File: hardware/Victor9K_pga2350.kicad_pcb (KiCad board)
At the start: 4 copper layers, 232.7 x 126.4 mm, 23 parts, among them IC1 74LVC1G14GW,125, J1 PICO DEBUG, J2 Micro_SD_Card, J4 DX07S016JA1R1500, J5 UART, SW1 BOOTSEL, U1 ESP32-S3-DevKitC

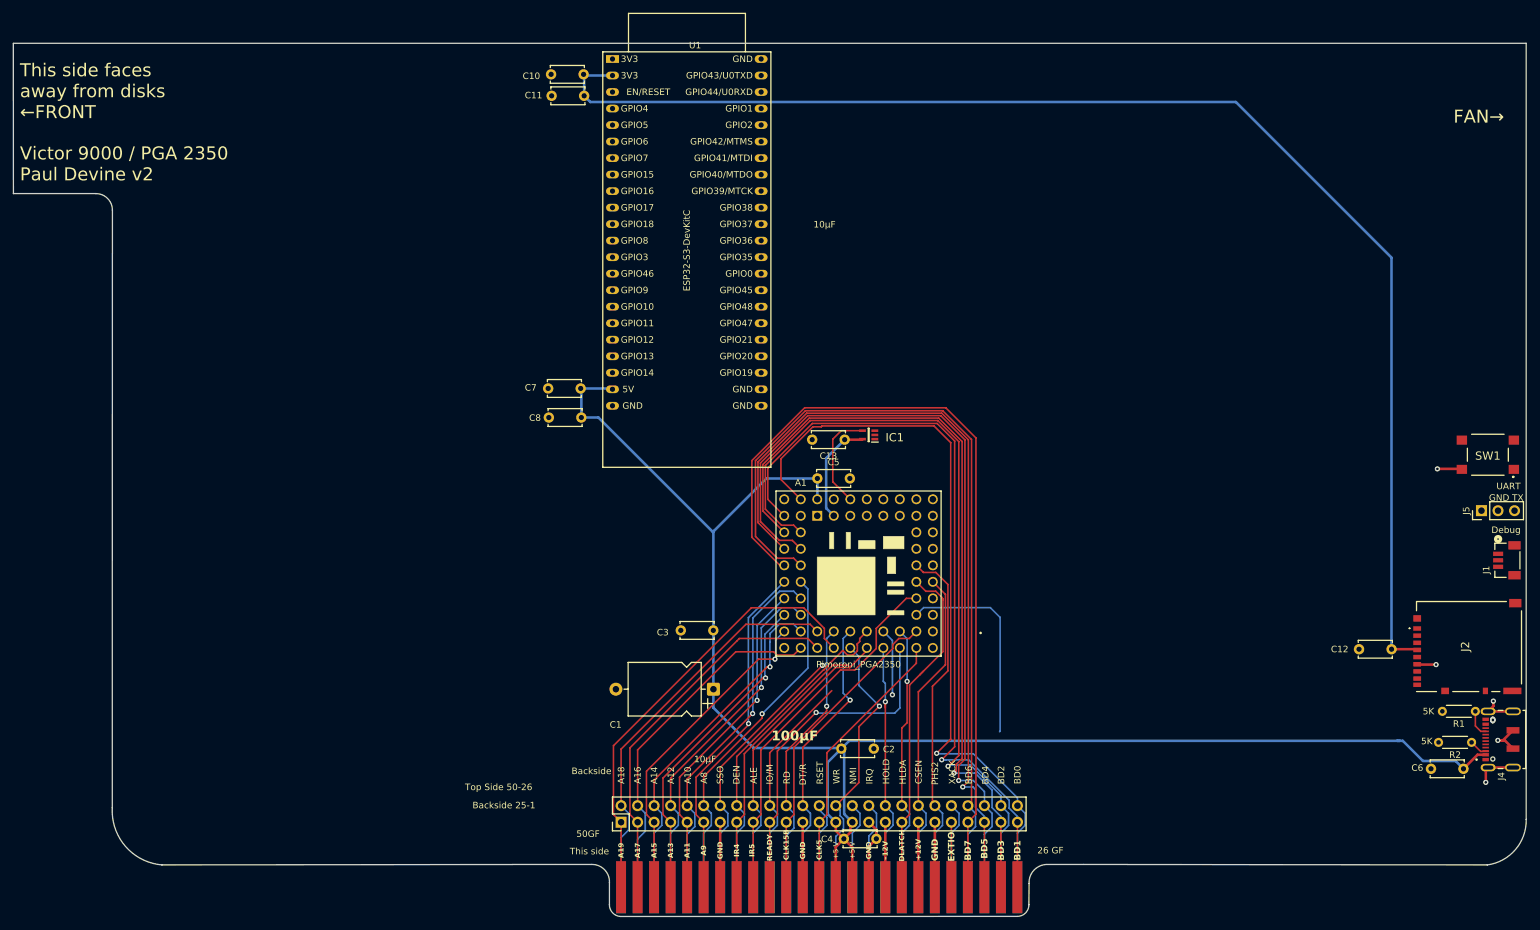
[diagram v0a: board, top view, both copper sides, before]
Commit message: reworked PCB for latest gpio configuration. added reset connect to 8088, adjusted SIP for SD card instead of SDIO. added UART RX and SIP breakout pins.
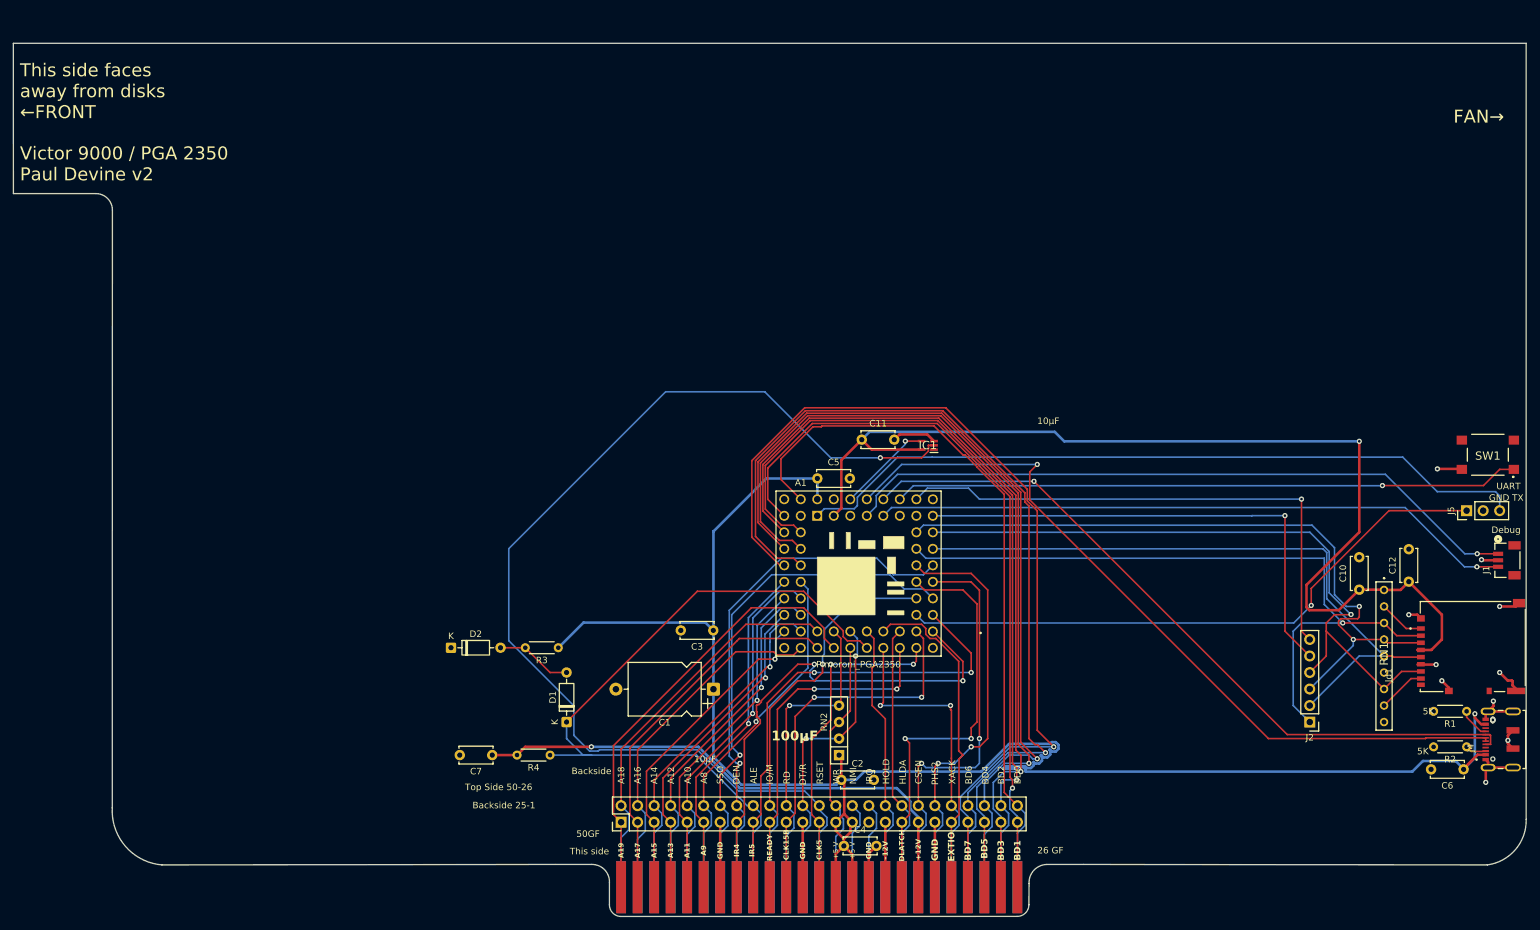
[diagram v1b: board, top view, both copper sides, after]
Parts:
- removed C13, C8: 0.1µF, Capacitor_THT:C_Disc_D5.0mm_W2.5mm_P5.00mm
- removed U1: ESP32-S3-DevKitC, Victor9000:ESP32-S3-DevKitC
- added D1: 1N4148, Diode_THT:D_DO-35_SOD27_P7.62mm_Horizontal, F.Cu at (118.1, 134.6)
- added D2: 1N4148, Diode_THT:D_DO-35_SOD27_P7.62mm_Horizontal, F.Cu at (100.3, 123.2)
- added J2: SPI Breakout, Connector_PinHeader_2.54mm:PinHeader_1x06_P2.54mm_Vertical, F.Cu at (232.4, 134.6)
- added R3: 470Ω, Resistor_THT:R_Axial_DIN0204_L3.6mm_D1.6mm_P5.08mm_Horizontal, F.Cu at (116.8, 123.2)
- added R4: 2.2KΩ, Resistor_THT:R_Axial_DIN0204_L3.6mm_D1.6mm_P5.08mm_Horizontal, F.Cu at (115.6, 139.7)
- added RN1: 47KΩ, Victor9000:4609X101473LF, F.Cu at (243.8, 114.3)
- added RN2: 2.7KΩ, Resistor_THT:R_Array_SIP4, F.Cu at (160.0, 139.7)
- C3: value 0.1µF -> 1µF
- C7: value 0.1µF -> .01µF
- IC1: value 74LVC1G14GW,125 -> SN74LVC1G04QDCKRQ1; footprint Victor9000:SOT65P212X110-5N -> Victor9000:SOT65P210X110-5N
- J4: value DX07S016JA1R1500 -> USB C DX07S016JA1R1500
- Jd1: renamed from J2; footprint Victor9000:DM3ATSFPEJM5 -> Victor9000:HRS_DM3AT-SF-PEJM5
- moved C10 143.2 mm to (240.0, 114.3), turned to 90 degrees
- moved C11 68.0 mm to (163.5, 91.2), turned to 0 degrees
- moved C7 58.0 mm to (106.7, 139.7)
- moved C12 10.7 mm to (247.7, 113.0), turned to 90 degrees
- moved IC1 9.23 mm to (173.7, 92.1)
- moved C2 4.80 mm to (160.4, 143.5)
- moved J5 2.29 mm to (256.5, 102.1)
- moved R1 1.35 mm to (256.5, 133.0)
- moved Jd1 1.14 mm to (257.5, 123.0)
- moved C4 1.09 mm to (160.8, 153.7)
- moved R2 1.03 mm to (256.5, 138.4)
- moved C6 0.09 mm to (256.1, 141.9)
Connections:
- net /NOT_RESET renamed /RUN
- A1 pad 25: /DEN -> /HOLD
- A1 pad 26: /HOLD -> /XACK
- A1 pad 33: /XACK -> /UART RX
- A1 pad 34: /IO/M -> /IR5
- A1 pad 35: /IR5 -> /IO/M
- A1 pad 40: /FN_MISO -> /DEN
- A1 pad 41: /FN_CS -> /SD_CS
- A1 pad 42: /FN_SCLK -> /SD_SCLK
- A1 pad 43: /FN_MOSI -> /SD_MOSI
- A1 pad 44: /FN_INT -> /SD_MISO
- A1 pad 45: unconnected-(A1-GPIO45-Pad45) -> /GPIO45
- A1 pad 46: /UART RX -> /GPIO46
- C7 pad 1: +5V -> -12V
- GF1 pad 32: /-12VLT -> -12V
- Jd1 pad 1: unconnected-(J2-DAT2-Pad1) -> /SD_DAT2
- Jd1 pad 3: /SD_MISO -> /SD_MOSI
- Jd1 pad 7: /SD_MOSI -> /SD_MISO
- Jd1 pad 8: unconnected-(J2-DAT1-Pad8) -> /SD_DAT1
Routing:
- net /RESET: track 13.5 -> 169.0 mm, vias 0 -> 1
- net Net-(A1-USB_DP): track 0.00 -> 120.2 mm, vias 0 -> 1
- net /UART TX: track 0.00 -> 114.2 mm
- net Net-(A1-USB_DM): track 0.00 -> 112.9 mm, vias 0 -> 1
- net /SD_CS: track 0.00 -> 110.5 mm, vias 0 -> 1
- net /SD_MOSI: track 0.00 -> 107.8 mm, vias 0 -> 2
- net /SWCLK: track 0.00 -> 105.8 mm, vias 0 -> 1
- net /SD_MISO: track 0.00 -> 105.7 mm, vias 0 -> 1
- net /SD_SCLK: track 0.00 -> 100.7 mm
- net /SWDIO: track 0.00 -> 98.9 mm, vias 0 -> 1
- net /BOOTSEL: track 0.00 -> 96.3 mm, vias 0 -> 1
- net /UART RX: track 0.00 -> 93.8 mm, vias 0 -> 1
- net /GPIO46: track 0.00 -> 82.8 mm, vias 0 -> 1
- net -12V: track 0.00 -> 82.0 mm, vias 0 -> 1
- net /GPIO45: track 0.00 -> 77.3 mm, vias 0 -> 1
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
